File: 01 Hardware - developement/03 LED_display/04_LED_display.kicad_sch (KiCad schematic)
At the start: 9 parts, among them J1 Conn_01x03_Male

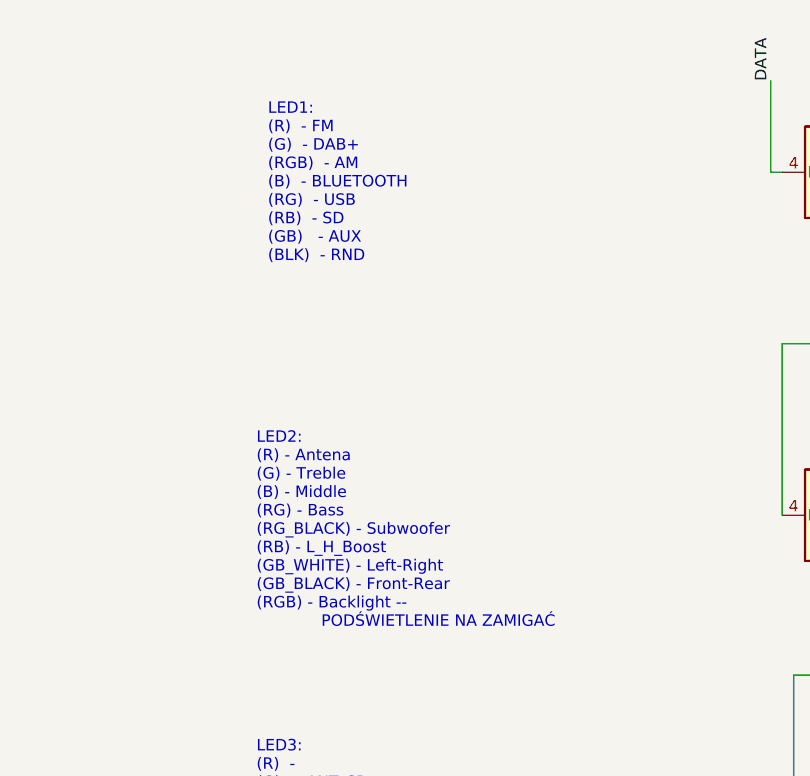
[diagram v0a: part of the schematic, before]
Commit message: wszystkie urządzenia. Trzeba zrobić opisy funkcji i porządek
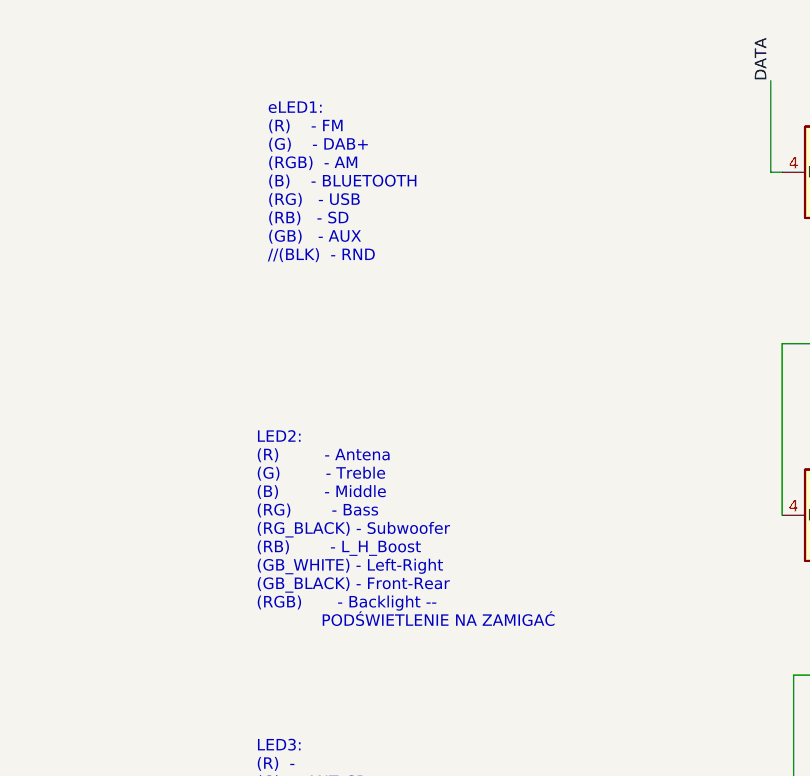
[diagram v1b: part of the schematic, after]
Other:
- note added: "eLED1: (R) - FM (G) - DAB+ (RGB) - AM (B) - BLUETOOTH (RG) - USB (RB) - SD (GB) - AUX //(BLK) - RND"
- note removed: "LED1: (R) - FM (G) - DAB+ (RGB) - AM (B) - BLUETOOTH (RG) - USB (RB) - SD (GB) - AUX (BLK) - RND"
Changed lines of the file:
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@@
     (stroke (width 0) (type default))
   )
-  (text "LED2:\n(R) - Antena\n(G) - Treble\n(B) - Middle\n(RG) - Bass\n(RG_BLACK) - Subwoofer\n(RB) - L_H_Boost\n(GB_WHITE) - Left-Right\n(GB_BLACK) - Front-Rear\n(RGB) - Backlight -- \n             PODŚWIETLENIE NA ZAMIGAĆ"
+  (text "LED2:\n(R)         - Antena\n(G)         - Treble\n(B)         - Middle\n(RG)        - Bass\n(RG_BLACK) - Subwoofer\n(RB)        - L_H_Boost\n(GB_WHITE) - Left-Right\n(GB_BLACK) - Front-Rear\n(RGB)       - Backlight -- \n             PODŚWIETLENIE NA ZAMIGAĆ"
     (at 171.45 96.52 0)
     (effects (font (size 1.27 1.27)) (justify left bottom))
@@
     (effects (font (size 1.27 1.27)) (justify left bottom))
   )
-  (text "LED1:\n(R)  - FM\n(G)  - DAB+\n(RGB)  - AM\n(B)  - BLUETOOTH\n(RG)  - USB\n(RB)  - SD\n(GB)   - AUX\n(BLK)  - RND\n"
+  (text "eLED1:\n(R)    - FM\n(G)    - DAB+\n(RGB)  - AM\n(B)    - BLUETOOTH\n(RG)   - USB\n(RB)   - SD\n(GB)   - AUX\n//(BLK)  - RND"
     (at 172.72 55.88 0)
     (effects (font (size 1.27 1.27)) (justify left bottom))

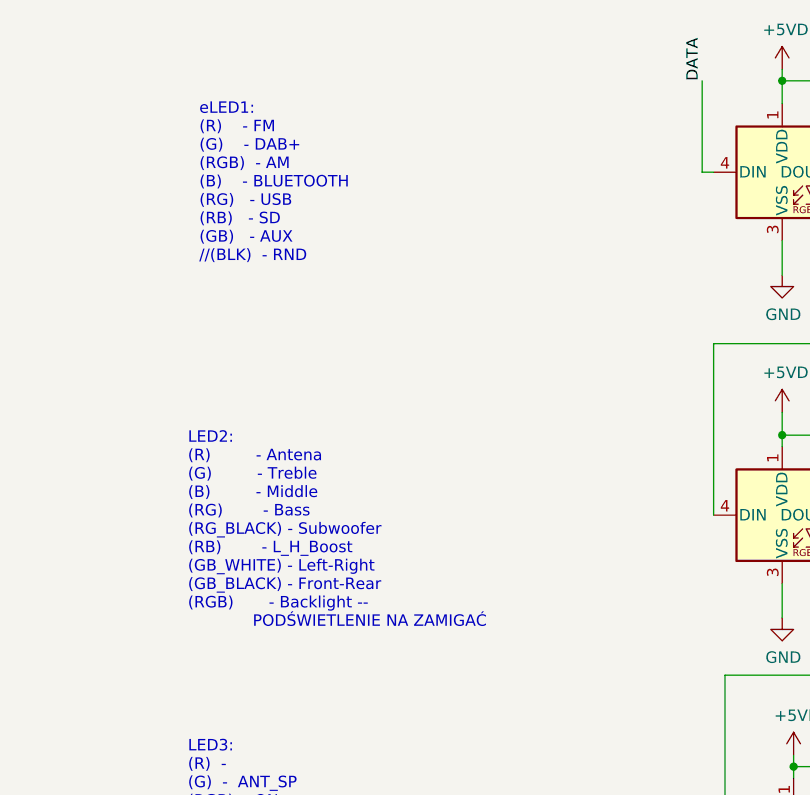
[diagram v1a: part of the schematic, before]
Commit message: poprawki związane z backlight
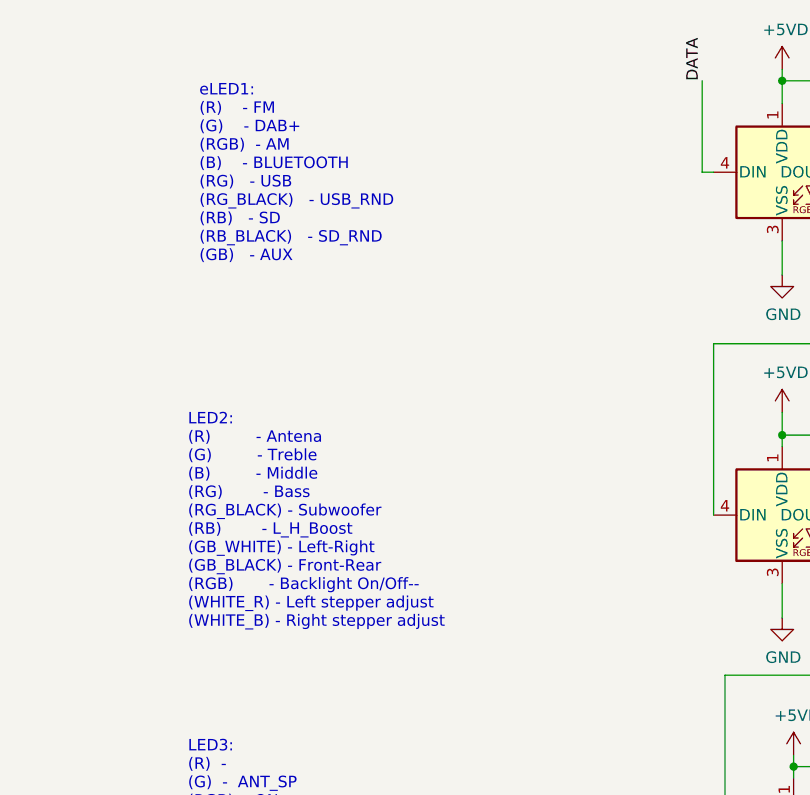
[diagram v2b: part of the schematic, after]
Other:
- note added: "LED2: (R) - Antena (G) - Treble (B) - Middle (RG) - Bass (RG_BLACK) - Subwoofer (RB) - L_H_Boost (GB_WHITE) - Left-Right (GB_BLACK) - Front-Rear (RGB) - Backlight On/Off-- (WHITE_R) - Left stepper adjust (WHITE_B) - Right stepper adjust"
- note added: "eLED1: (R) - FM (G) - DAB+ (RGB) - AM (B) - BLUETOOTH (RG) - USB (RG_BLACK) - USB_RND (RB) - SD (RB_BLACK) - SD_RND (GB) - AUX"
- note removed: "LED2: (R) - Antena (G) - Treble (B) - Middle (RG) - Bass (RG_BLACK) - Subwoofer (RB) - L_H_Boost (GB_WHITE) - Left-Right (GB_BLACK) - Front-Rear (RGB) - Backlight -- PODŚWIETLENIE NA ZAMIGAĆ"
- note removed: "eLED1: (R) - FM (G) - DAB+ (RGB) - AM (B) - BLUETOOTH (RG) - USB (RB) - SD (GB) - AUX //(BLK) - RND"
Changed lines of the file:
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@@
     (stroke (width 0) (type default))
   )
-  (text "LED2:\n(R)         - Antena\n(G)         - Treble\n(B)         - Middle\n(RG)        - Bass\n(RG_BLACK) - Subwoofer\n(RB)        - L_H_Boost\n(GB_WHITE) - Left-Right\n(GB_BLACK) - Front-Rear\n(RGB)       - Backlight -- \n             PODŚWIETLENIE NA ZAMIGAĆ"
+  (text "LED2:\n(R)         - Antena\n(G)         - Treble\n(B)         - Middle\n(RG)        - Bass\n(RG_BLACK) - Subwoofer\n(RB)        - L_H_Boost\n(GB_WHITE) - Left-Right\n(GB_BLACK) - Front-Rear\n(RGB)       - Backlight On/Off--\n(WHITE_R) - Left stepper adjust\n(WHITE_B) - Right stepper adjust\n"
     (at 171.45 96.52 0)
     (effects (font (size 1.27 1.27)) (justify left bottom))
@@
     (effects (font (size 1.27 1.27)) (justify left bottom))
   )
-  (text "eLED1:\n(R)    - FM\n(G)    - DAB+\n(RGB)  - AM\n(B)    - BLUETOOTH\n(RG)   - USB\n(RB)   - SD\n(GB)   - AUX\n//(BLK)  - RND"
+  (text "eLED1:\n(R)    - FM\n(G)    - DAB+\n(RGB)  - AM\n(B)    - BLUETOOTH\n(RG)   - USB\n(RG_BLACK)   - USB_RND\n(RB)   - SD\n(RB_BLACK)   - SD_RND\n(GB)   - AUX"
     (at 172.72 55.88 0)
     (effects (font (size 1.27 1.27)) (justify left bottom))
